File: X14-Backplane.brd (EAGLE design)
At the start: 88.9 x 139.7 mm, 27 parts, among them J2 PXC-PTSM-04-RA-1778641, J3 PXC-8-RA-1778683, J8 PXC-8-RA-1778683

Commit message: some adjustments
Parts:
- moved R8 71.6 mm to (78.3, 20.3), turned to 180 degrees
- moved R7 71.6 mm to (78.2, 17.5), turned to 0 degrees
- moved C4 65.5 mm to (74.8, 18.8), turned to 180 degrees
- moved J2 5.79 mm to (2.03, 51.3)
- moved J8 4.44 mm to (93.0, 62.0)
- moved J3 4.32 mm to (-3.81, 125.2)
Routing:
- net 12V_L: track 107.6 -> 39.9 mm
- net 3V3: track 394.4 -> 412.9 mm
- net NRST: track 108.2 -> 112.5 mm
- net PROG_1: track 13.0 -> 17.3 mm
- net SWCLK_IN: track 19.5 -> 22.8 mm
- net PROG_3: track 18.0 -> 21.2 mm
- net SWDIO_IN: track 25.5 -> 28.7 mm
- net GND_L: track 2.08 -> 3.66 mm, vias 18 -> 26
- net CAN_L: track 227.8 -> 229.2 mm
- net SWCLK_3: track 107.1 -> 108.2 mm
- net CAN_H: track 224.0 -> 224.8 mm
- net SOL5_1: track 61.6 -> 62.3 mm
- net SOL4_1: track 55.5 -> 56.2 mm
- net SOL3_1: track 49.4 -> 50.2 mm
- net SOL2_1: track 43.3 -> 44.1 mm
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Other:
- board text added: "Reserved Space for SMBUS->CAN Board (process Bricks data)"
- board text removed: "Reserved Space for SMBUS->I2C Board"

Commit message: afawevvew
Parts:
- added U$10: BACKPLANE->DATACONV, CONN, DataConversion-Backplane Connector- SAMTEC CLT-107-01-F-D:SAMTEC-CLT-107-01-X-D-BACKPLANE
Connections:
- new net +3V3: U$10.1
- new net ALERT1: U$10.14
- new net ALERT2: U$10.12
- new net GND: U$10.2, U$10.3
- new net SWCLK: U$10.8
- new net SWDIO: U$10.6
- net C2_1: now also U$10.9
- net C2_2: now also U$10.7
- net CAN_H: now also U$10.10
- net CAN_L: now also U$10.11
- net CLK: now also U$10.5
- net DATA: now also U$10.4
- net NRST: now also U$10.13
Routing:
- net NRST: track 112.5 -> 119.6 mm
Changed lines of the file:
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@@
 <?xml version="1.0" encoding="utf-8"?>
 <!DOCTYPE eagle SYSTEM "eagle.dtd">
-<eagle version="9.5.0">
+<eagle version="9.6.2">
 <drawing>
 <settings>
@@
 <element name="J8" library="Phoenix Contact PTSM 8 pin" package="PXC-8-RA-1778683" package3d_urn="urn:adsk.eagle:package:25224885/2" value="PXC-8-RA-1778683" x="92.964" y="61.976" smashed="yes" rot="R90"/>
 <element name="U$9" library="PI-SHIELD, Solenoid-Backplane" package="IPL7X2" value="7X_CONN" x="80.772" y="36.576" smashed="yes" rot="R270"/>
+<element name="U$10" library="CONN, DataConversion-Backplane Connector- SAMTEC CLT-107-01-F-D" package="SAMTEC-CLT-107-01-X-D-BACKPLANE" value="BACKPLANE-&gt;DATACONV" x="69.088" y="121.92" smashed="yes">
+<attribute name="NAME" x="62.173" y="125.237" size="1.016" layer="25"/>
+</element>
 </elements>
 <signals>
@@
 <wire x1="82.042" y1="19.304" x2="80.264" y2="17.526" width="0.254" layer="1"/>
 <wire x1="80.264" y1="17.526" x2="79.082" y2="17.526" width="0.254" layer="1"/>
+<contactref element="U$10" pad="10"/>
+<wire x1="71.088" y1="120.409" x2="7.112" y2="12.954" width="0" layer="19" extent="1-1"/>
 </signal>
 <signal name="CAN_L">
@@
 <wire x1="83.2866" y1="20.3454" x2="79.1074" y2="20.3454" width="0.254" layer="1"/>
 <wire x1="84.328" y1="19.304" x2="83.2866" y2="20.3454" width="0.254" layer="1"/>
+<contactref element="U$10" pad="11"/>
+<wire x1="73.088" y1="123.431" x2="7.493" y2="11.557" width="0" layer="19" extent="1-1"/>
 </signal>
 <signal name="5V">
@@
 <wire x1="3.556" y1="94.028" x2="3.556" y2="90.258" width="0.254" layer="1"/>
 <wire x1="3.556" y1="94.028" x2="3.858" y2="93.726" width="0.254" layer="1"/>
-<wire x1="3.858" y1="93.726" x2="11.43" y2="93.726" width="0.254" layer="1"/>
+<wire x1="3.858" y1="93.726" x2="6.604" y2="93.726" width="0.254" layer="1"/>
 <via x="11.43" y="93.726" extent="1-16" drill="0.35"/>
+<wire x1="6.604" y1="93.726" x2="11.43" y2="93.726" width="0.254" layer="1"/>
 <wire x1="12.312" y1="109.22" x2="11.43" y2="109.22" width="0.254" layer="1"/>
 <via x="11.43" y="109.22" extent="1-16" drill="0.35"/>
@@
 <wire x1="10.16" y1="22.352" x2="11.804" y2="22.352" width="0.254" layer="1"/>
 <wire x1="10.16" y1="65.786" x2="10.16" y2="22.352" width="0.254" layer="16"/>
-<wire x1="3.556" y1="94.028" x2="7.74" y2="100.33" width="0" layer="19" extent="1-1"/>
+<wire x1="6.604" y1="93.726" x2="6.604" y2="99.194" width="0.254" layer="1"/>
+<wire x1="6.604" y1="99.194" x2="7.74" y2="100.33" width="0.254" layer="1"/>
+<contactref element="U$10" pad="13"/>
+<wire x1="75.088" y1="123.431" x2="10.16" y2="22.352" width="0" layer="19" extent="1-1"/>
 </signal>
 <signal name="ESCID_1">
@@
 <signal name="DATA">
 <contactref element="U$4" pad="08"/>
+<contactref element="U$10" pad="4"/>
+<wire x1="65.088" y1="120.409" x2="80.518" y2="116.332" width="0" layer="19" extent="1-1"/>
 </signal>
 <signal name="ALERT_1">
@@
 <signal name="C2_2">
 <contactref element="U$4" pad="13"/>
+<contactref element="U$10" pad="7"/>
+<wire x1="69.088" y1="123.431" x2="80.518" y2="129.032" width="0" layer="19" extent="1-1"/>
 </signal>
 <signal name="C2_1">
 <contactref element="U$4" pad="12"/>
+<contactref element="U$10" pad="9"/>
+<wire x1="71.088" y1="123.431" x2="80.518" y2="126.492" width="0" layer="19" extent="1-1"/>
 </signal>
 <signal name="CLK">
 <contactref element="U$4" pad="11"/>
+<contactref element="U$10" pad="5"/>
+<wire x1="67.088" y1="123.431" x2="80.518" y2="123.952" width="0" layer="19" extent="1-1"/>
 </signal>
 <signal name="SOL2_1">
@@
 <wire x1="83.5914" y1="42.6974" x2="85.9282" y2="40.3606" width="0.762" layer="16"/>
 </signal>
+<signal name="GND">
+<contactref element="U$10" pad="3"/>
+<contactref element="U$10" pad="2"/>
+<wire x1="65.088" y1="123.431" x2="63.088" y2="120.409" width="0" layer="19" extent="1-1"/>
+</signal>
+<signal name="+3V3">
+<contactref element="U$10" pad="1"/>
+</signal>
+<signal name="SWDIO">
+<contactref element="U$10" pad="6"/>
+</signal>
+<signal name="SWCLK">
+<contactref element="U$10" pad="8"/>
+</signal>
+<signal name="ALERT2">
+<contactref element="U$10" pad="12"/>
+</signal>
+<signal name="ALERT1">
+<contactref element="U$10" pad="14"/>
+</signal>
 </signals>

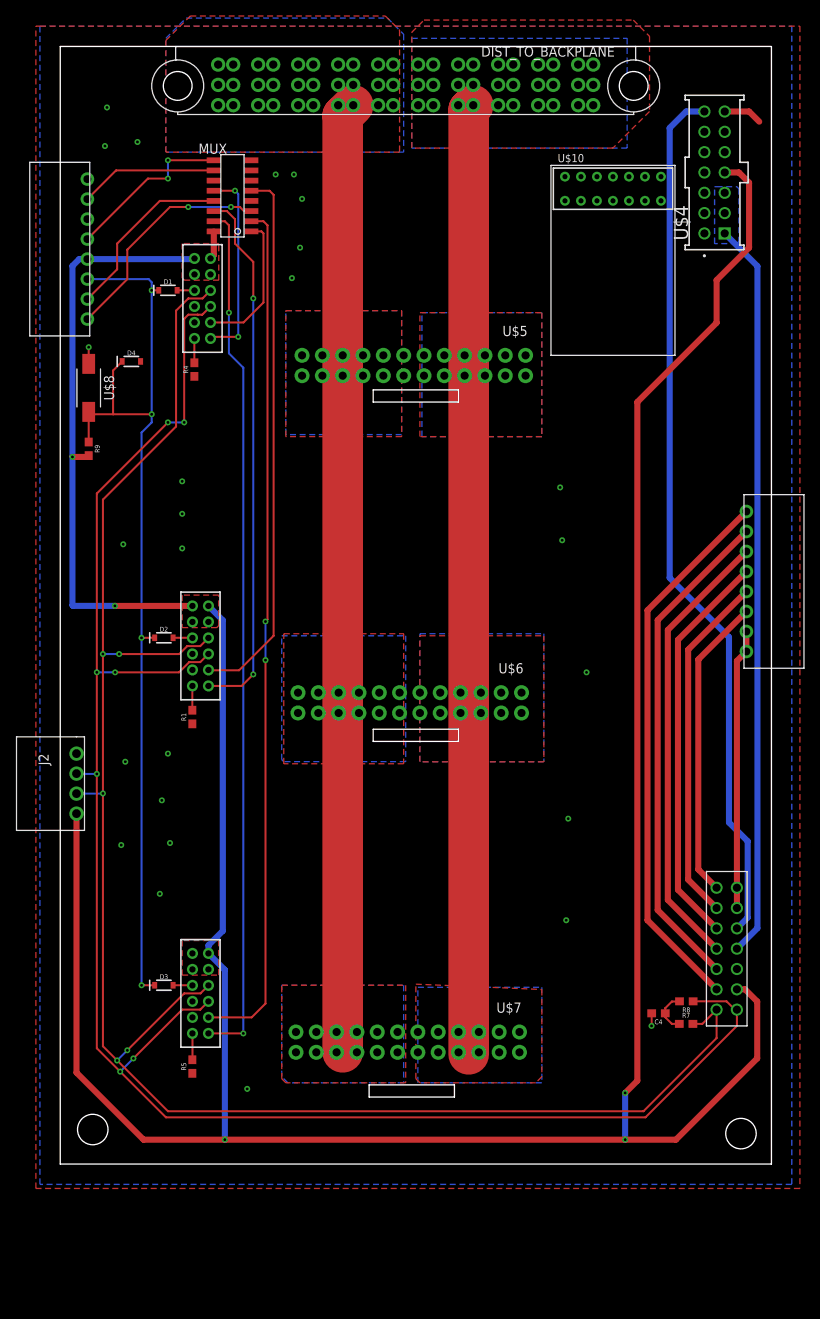
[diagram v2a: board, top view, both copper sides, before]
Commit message: Implemented conversion board
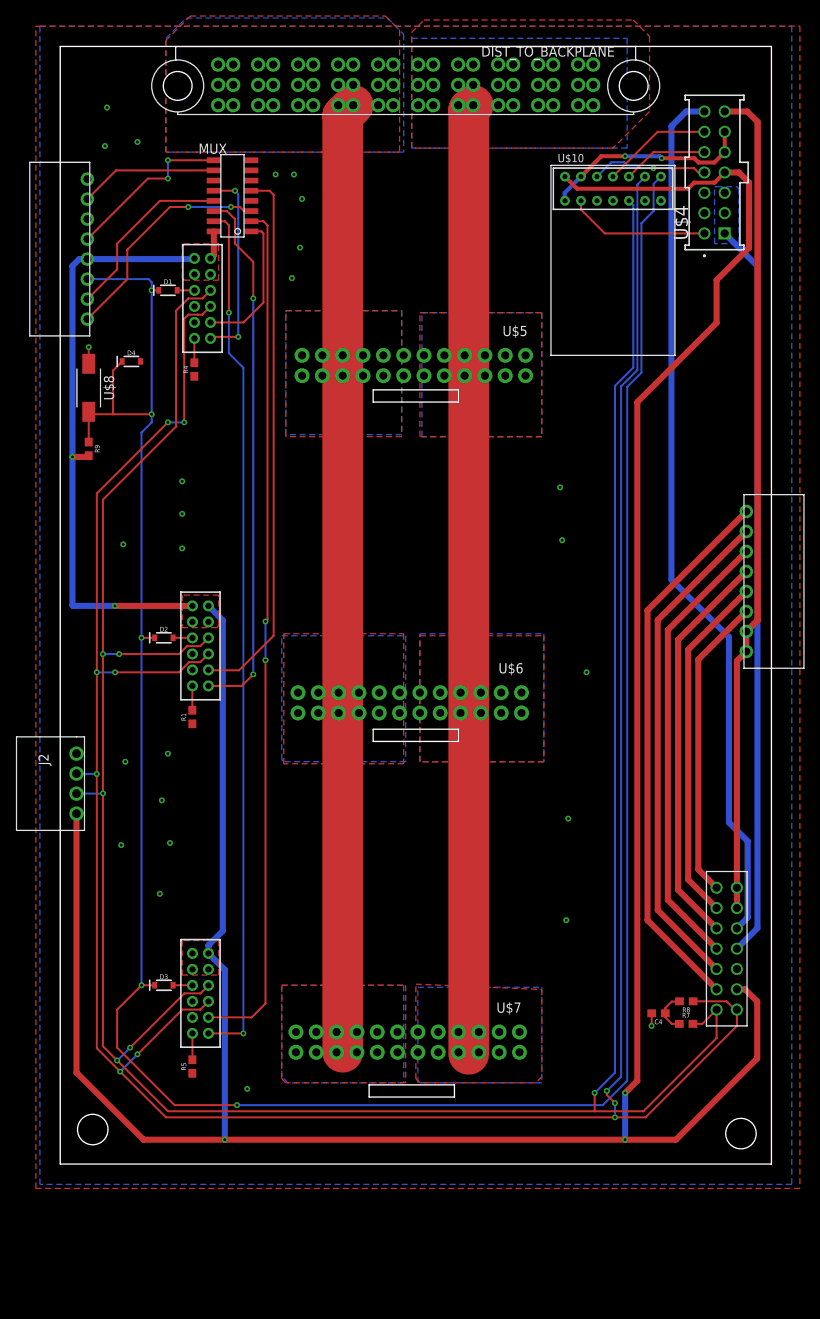
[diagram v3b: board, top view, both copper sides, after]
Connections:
- removed net +3V3: U$10.1
- removed net GND: U$10.2, U$10.3
- net 3V3: now also U$10.1
- net GND_L: now also U$10.2, U$10.3
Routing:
- net NRST: track 119.6 -> 311.4 mm, vias 4 -> 5
- net CAN_L: track 229.2 -> 349.2 mm, vias 7 -> 10
- net CAN_H: track 224.8 -> 340.9 mm, vias 5 -> 6
- net 12V_L: track 39.9 -> 104.0 mm
- net GND_L: track 3.66 -> 30.0 mm, vias 26 -> 28
- net 3V3: track 412.9 -> 434.3 mm
- net DATA: track 0.00 -> 17.8 mm
- net CLK: track 0.00 -> 14.7 mm, vias 0 -> 1
- net C2_2: track 0.00 -> 13.8 mm
- net C2_1: track 0.00 -> 10.7 mm
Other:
- board text removed: "Reserved Space for SMBUS->CAN Board (process Bricks data)"

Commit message: second round of edits to bkplane
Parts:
- moved D4 58.2 mm to (65.5, 113.8)
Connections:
- removed net ALERT1: U$10.14
- removed net ALERT2: U$10.12
- removed net SWCLK: U$10.8
- removed net SWDIO: U$10.6
- net ALERT_1: now also U$10.14
- net ALERT_2: now also U$10.12
- net NRST: no longer U$10.13
- net NRST_4: now also U$10.13
- net SWCLK_4: now also U$10.8
- net SWDIO_4: now also U$10.6
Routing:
- net NRST: track 311.4 -> 181.4 mm, vias 5 -> 8
- net SWCLK_4: track 0.00 -> 55.8 mm, vias 0 -> 1
- net SWDIO_4: track 0.00 -> 49.1 mm, vias 0 -> 3
- net NRST_4: track 0.00 -> 17.2 mm, vias 0 -> 1
- net ALERT_2: track 0.00 -> 11.2 mm, vias 0 -> 1
- net ALERT_1: track 0.00 -> 6.07 mm
- net CAN_H: track 340.9 -> 340.2 mm, vias 6 -> 8
- net 5V: track 92.2 -> 92.8 mm
- net GND_L: vias 28 -> 34

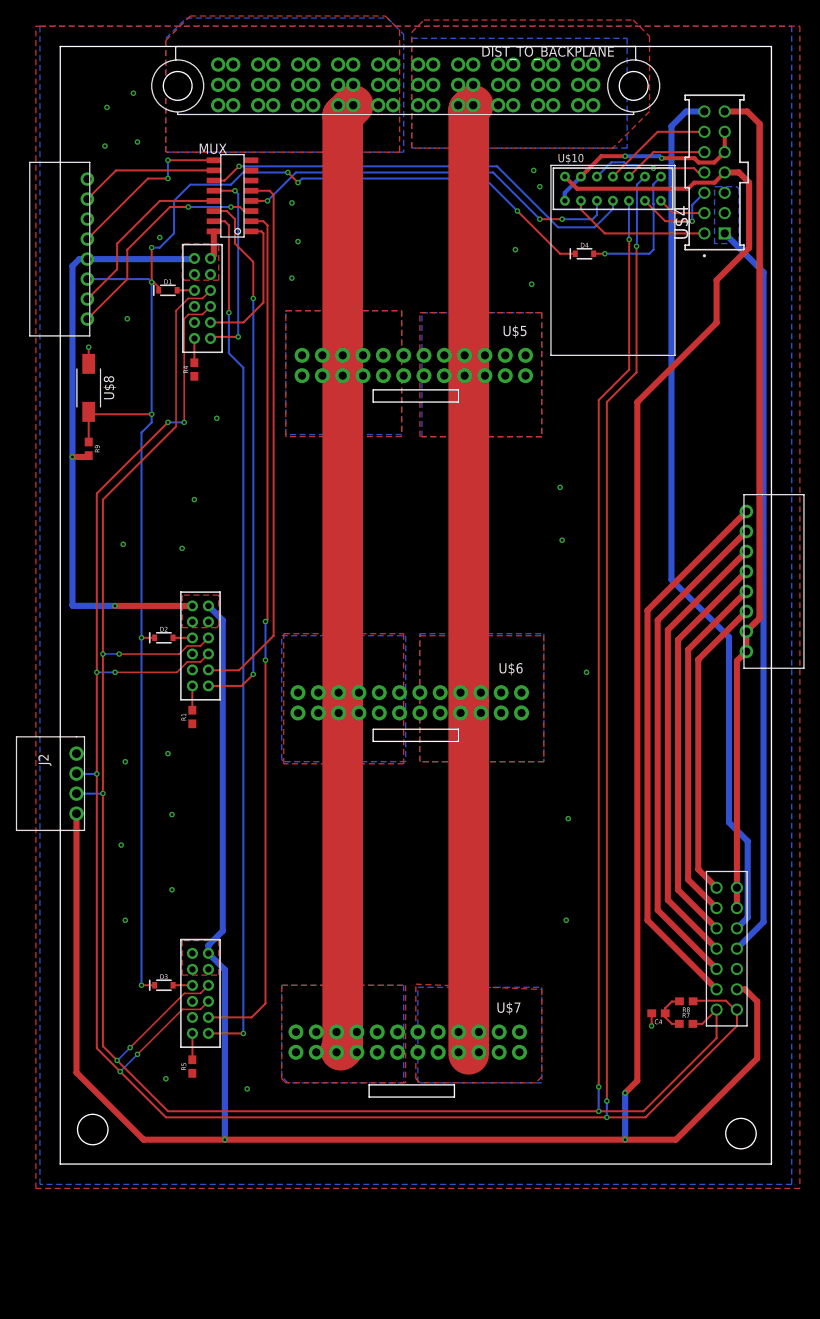
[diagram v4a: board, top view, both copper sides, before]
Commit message: added ESC adapter holes and some capacitors
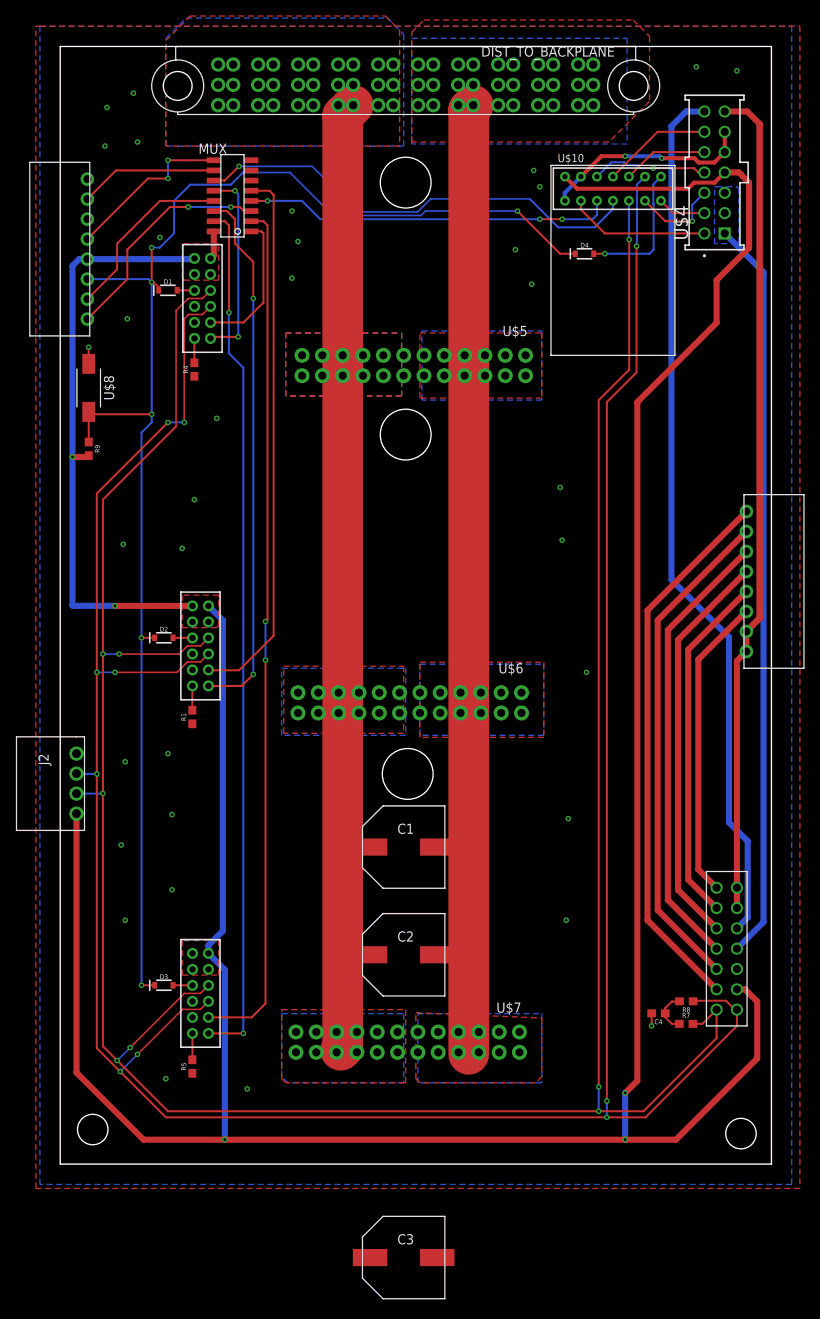
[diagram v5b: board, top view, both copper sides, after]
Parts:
- added C1, C2, C3: 330uF, CAP, aluminin-capacitor-brick-UCM1H331MNL1GS:CAPAE1030X1050N
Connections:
- net 12V: now also C1.+, C2.+, C3.+
- net 12VGND: now also C1.-, C2.-, C3.-
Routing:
- net SWDIO_4: track 49.1 -> 46.1 mm
- net SWCLK_4: track 55.8 -> 57.1 mm
- net NRST: vias 8 -> 6
- net GND_L: vias 34 -> 36
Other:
- outline, holes or cut-outs redrawn

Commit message: TODO: Fix CAN line, Silkcreen
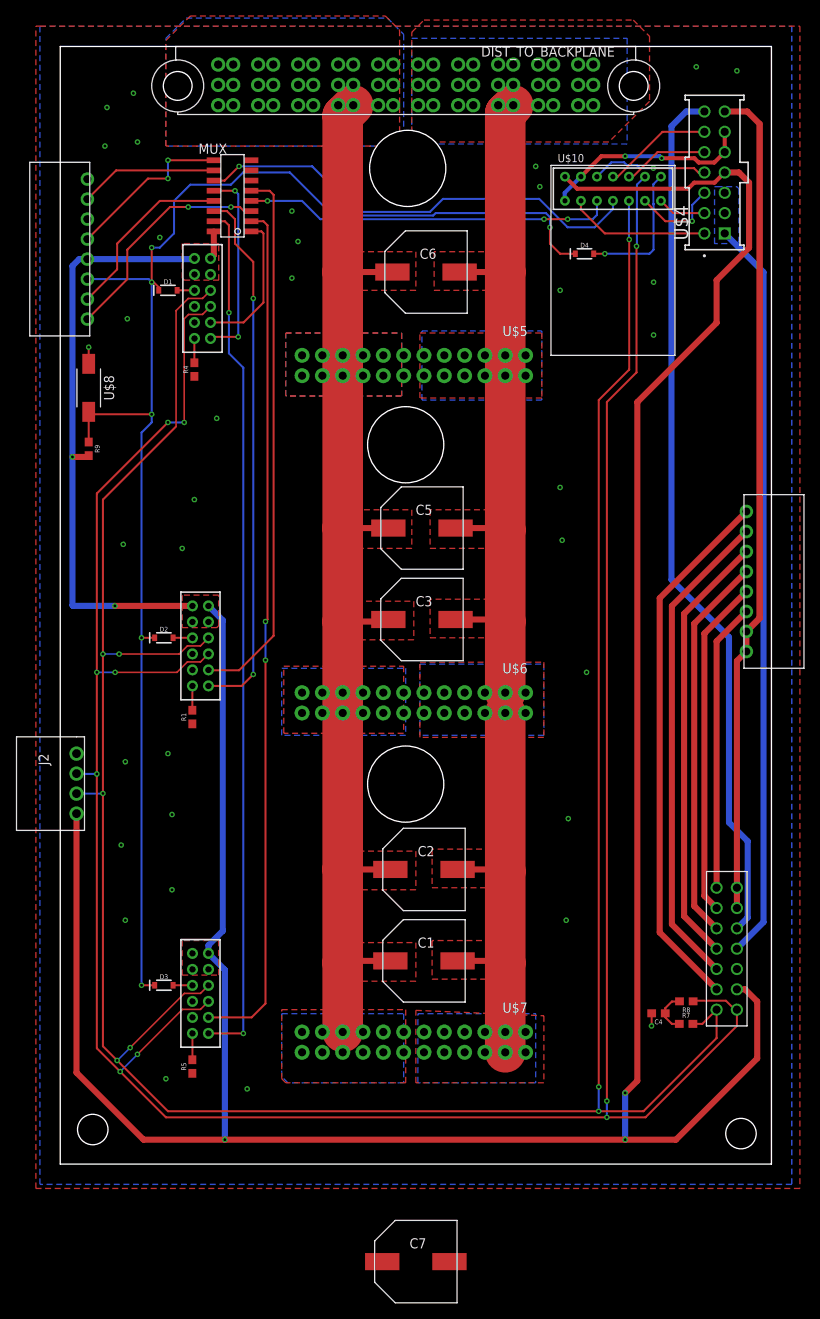
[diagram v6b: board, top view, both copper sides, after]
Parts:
- added C5, C6, C7: 330uF, CAP, aluminin-capacitor-brick-UCM1H331MNL1GS:CAPAE1030X1050N
- moved C3 79.8 mm to (45.2, 68.1)
- moved C1 14.4 mm to (45.5, 25.4)
- moved C2 11.0 mm to (45.5, 36.8)
- moved U$7 0.76 mm to (95.2, 52.8)
- moved U$6 0.51 mm to (95.2, 95.2)
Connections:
- net 12V: now also C5.+, C6.+, C7.+
- net 12VGND: now also C5.-, C6.-, C7.-
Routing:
- net 12VGND: track 118.9 -> 146.7 mm
- net 12V: track 118.8 -> 146.2 mm
- net SOL1_1: track 38.0 -> 36.1 mm
- net NRST: track 181.4 -> 183.1 mm
- net SOL3_1: track 50.2 -> 48.5 mm
- net SOL2_1: track 44.1 -> 42.4 mm
- net SOL4_1: track 56.2 -> 54.6 mm
- net SOL5_1: track 62.3 -> 60.9 mm
- net SOL6_1: track 68.4 -> 67.2 mm
- net GND_L: vias 36 -> 37
